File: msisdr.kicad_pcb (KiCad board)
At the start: 2 copper layers, 67 parts, among them J1 USB_OTG, J10 GPIO2, J11 GPIO3, J2 SMA_0_30MHZ, J3 SMA_30_60MHZ, J4 SMA_VHF2, J5 SMA_UHF, J6 SMA_VHF1, J7 VCC_GPIO, J8 GPIO0, J9 GPIO1, U1 msi2500, U2 msi001, U3 LP5900SDX-2.8, U4 AP7313-30SAG, Y1 24MHz

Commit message: update and fix bug
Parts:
- removed C39, C40, C41, C42: 10uF, Capacitors_SMD:C_0805
- added C23: 6800pF, Capacitors_SMD:C_0603, F.Cu at (152.2, 132.7)
- added C37: 10uF, Capacitors_SMD:C_0805, F.Cu at (145.6, 123.8)
- added D1: D, Diodes_SMD:D_0805, F.Cu at (159.9, 84.2)
- C10: value 10nF -> 18pF
- C15: value 100nF -> 10nF
- C17: value 1uF -> 100nF; footprint Capacitors_SMD:C_0805 -> Capacitors_SMD:C_0603
- C18: value 10nF -> 1uF; footprint Capacitors_SMD:C_0603 -> Capacitors_SMD:C_0805
- C21: value 6800pF -> 10nF
- C26: value 470nF -> 10nF; footprint Capacitors_SMD:C_0805 -> Capacitors_SMD:C_0603
- C27: value 1nF -> 470nF; footprint Capacitors_SMD:C_0603 -> Capacitors_SMD:C_0805
- C28: value 160pF -> 1nF
- C29: value 3.9pF -> 56pF
- C30: value 56pF -> 3.9pF
- C32: value 56pF -> 39pF
- C33: value 39pF -> 160pF
- C34: value 10uF -> 56pF; footprint Capacitors_SMD:C_0805 -> Capacitors_SMD:C_0603
- C35: value 10uF -> 100uF; footprint Capacitors_SMD:C_0805 -> Capacitors_THT:CP_Radial_D5.0mm_P2.50mm
- C7: value 1uF -> 10uF
- C8: value 18pF -> 1uF; footprint Capacitors_SMD:C_0603 -> Capacitors_SMD:C_0805
- J1: value USB_OTG -> VCC_GPIO; footprint Connectors:USB_Mini-B -> Connectors:Pin_d0.7mm_L6.5mm_W1.8mm_FlatFork
- J10: value GPIO2 -> SMA_VHF1; footprint Connectors:Pin_d0.7mm_L6.5mm_W1.8mm_FlatFork -> sma:SMA_OPL_EMPTYHEAD
- J11: value GPIO3 -> USB_OTG; footprint Connectors:Pin_d0.7mm_L6.5mm_W1.8mm_FlatFork -> Connectors:USB_Mini-B
- J2: value SMA_0_30MHZ -> GPIO0; footprint sma:SMA_OPL_EM -> Connectors:Pin_d0.7mm_L6.5mm_W1.8mm_FlatFork
- J3: value SMA_30_60MHZ -> GPIO1; footprint sma:SMA_OPL_EM -> Connectors:Pin_d0.7mm_L6.5mm_W1.8mm_FlatFork
- J4: value SMA_VHF2 -> GPIO2; footprint sma:SMA_OPL_EMPTYHEAD -> Connectors:Pin_d0.7mm_L6.5mm_W1.8mm_FlatFork
- J5: value SMA_UHF -> GPIO3; footprint sma:SMA_OPL_EMPTYHEAD -> Connectors:Pin_d0.7mm_L6.5mm_W1.8mm_FlatFork
- J6: value SMA_VHF1 -> SMA_0_30MHZ; footprint sma:SMA_OPL_EMPTYHEAD -> sma:SMA_OPL_EM
- J7: value VCC_GPIO -> SMA_30_60MHZ; footprint Connectors:Pin_d0.7mm_L6.5mm_W1.8mm_FlatFork -> sma:SMA_OPL_EM
- J8: value GPIO0 -> SMA_VHF2; footprint Connectors:Pin_d0.7mm_L6.5mm_W1.8mm_FlatFork -> sma:SMA_OPL_EMPTYHEAD
- J9: value GPIO1 -> SMA_UHF; footprint Connectors:Pin_d0.7mm_L6.5mm_W1.8mm_FlatFork -> sma:SMA_OPL_EMPTYHEAD
- L2: value 270nH -> 330nH
- L4: value 150nH -> 270nH
- L5: value 330nH -> 150nH
- moved J7 120.0 mm to (169.0, 159.8), turned to 90 degrees
- moved J10 108.6 mm to (178.3, 148.8)
- moved J8 105.7 mm to (156.9, 154.1)
- moved J9 103.1 mm to (167.2, 147.7)
- moved J6 84.6 mm to (147.8, 159.0), turned to 90 degrees
- moved J1 83.1 mm to (152.2, 132.7), turned to 0 degrees
- moved J5 68.6 mm to (152.2, 132.7)
- moved Y1 66.6 mm to (179.5, 136.6)
- moved U2 65.0 mm to (135.0, 158.5)
- moved C35 62.0 mm to (161.9, 89.4)
- moved C30 61.5 mm to (155.8, 132.6)
- moved C3 59.9 mm to (145.7, 139.1)
- moved C29 59.2 mm to (148.2, 132.5)
- moved C8 58.6 mm to (173.5, 126.6)
- moved C26 57.1 mm to (152.2, 132.7)
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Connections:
- C10 pad 2: VRF -> Net-(C10-Pad2)
- C12 pad 2: Net-(C12-Pad2) -> VRF
- C16 pad 1: HFPORT -> GND
- C17 pad 1: GND -> HFPORT
- C17 pad 2: VRF -> Net-(C17-Pad2)
- C18 pad 2: Net-(C18-Pad2) -> VRF
- C19 pad 2: VRF -> Net-(C19-Pad2)
- C20 pad 2: VDDI -> VRF
- C21 pad 1: Net-(C21-Pad1) -> GND
- C21 pad 2: Net-(C21-Pad2) -> VDDI
- C22 pad 2: Net-(C21-Pad2) -> Net-(C22-Pad2)
- C25 pad 1: Net-(C21-Pad1) -> GND
- C25 pad 2: GND -> VRF
- C26 pad 1: Net-(C26-Pad1) -> Net-(C22-Pad1)
- C26 pad 2: Net-(C26-Pad2) -> GND
- C27 pad 1: Net-(C26-Pad1) -> Net-(C27-Pad1)
- C27 pad 2: Net-(C26-Pad2) -> Net-(C27-Pad2)
- C28 pad 1: GND -> Net-(C27-Pad1)
- C28 pad 2: Net-(C28-Pad2) -> Net-(C27-Pad2)
- C29 pad 1: Net-(C29-Pad1) -> GND
- C29 pad 2: Net-(C29-Pad2) -> Net-(C27-Pad2)
- C30 pad 1: GND -> Net-(C30-Pad1)
- C30 pad 2: Net-(C26-Pad2) -> Net-(C30-Pad2)
- C32 pad 1: GND -> HFPORT
- C32 pad 2: HFPORT -> Net-(C30-Pad1)
- C33 pad 1: HFPORT -> GND
- C33 pad 2: Net-(C29-Pad1) -> Net-(C33-Pad2)
- C34 pad 1: VDIG -> GND
- C34 pad 2: GND -> HFPORT
- C36 pad 1: VDIG -> VRF
- C38 pad 1: VDIG -> Net-(C38-Pad1)
- C7 pad 1: Net-(C7-Pad1) -> VDIG
- C8 pad 1: GND -> Net-(C8-Pad1)
- C8 pad 2: Net-(C8-Pad2) -> GND
- J1 pad 1: Net-(C42-Pad1) -> Net-(J1-Pad1)
- J10 pad 1: Net-(J10-Pad1) -> VHF_50_120MHZ
- J11 pad 1: Net-(J11-Pad1) -> Net-(C38-Pad1)
- J2 pad 1: Net-(C26-Pad1) -> Net-(J2-Pad1)
- J4 pad 1: VHF_120_250MHZ -> Net-(J4-Pad1)
- J5 pad 1: UHF_400_1000MHZ -> Net-(J5-Pad1)
- J6 pad 1: VHF_50_120MHZ -> Net-(C27-Pad1)
- J8 pad 1: Net-(J8-Pad1) -> VHF_120_250MHZ
- J9 pad 1: Net-(J9-Pad1) -> UHF_400_1000MHZ
- L1 pad 1: Net-(C29-Pad2) -> Net-(C30-Pad2)
- L1 pad 2: Net-(J3-Pad1) -> Net-(J7-Pad1)
- L2 pad 1: Net-(L2-Pad1) -> Net-(C30-Pad1)
- L2 pad 2: Net-(C28-Pad2) -> Net-(C30-Pad2)
- L3 pad 1: Net-(C28-Pad2) -> Net-(C31-Pad2)
- L3 pad 2: Net-(C26-Pad2) -> Net-(C27-Pad2)
- L4 pad 1: Net-(C31-Pad2) -> Net-(L4-Pad1)
- L4 pad 2: Net-(L2-Pad1) -> Net-(C31-Pad2)
- L5 pad 1: Net-(C29-Pad1) -> Net-(C33-Pad2)
- L5 pad 2: Net-(C29-Pad2) -> Net-(L4-Pad1)
- L6 pad 2: Net-(C31-Pad2) -> Net-(C33-Pad2)
- R2 pad 1: Net-(C21-Pad1) -> Net-(C22-Pad1)
- R2 pad 2: Net-(C22-Pad1) -> Net-(C23-Pad1)
- U1 pad 1: Net-(J7-Pad1) -> Net-(J1-Pad1)
- U1 pad 16: Net-(C7-Pad1) -> Net-(C8-Pad1)
- U1 pad 19: USB-DP -> USB_DP
- U1 pad 2: Net-(J8-Pad1) -> Net-(J2-Pad1)
- U1 pad 20: USB-DM -> USB_DM
- U1 pad 22: Net-(C9-Pad2) -> Net-(C10-Pad2)
- U1 pad 23: Net-(C8-Pad2) -> Net-(C9-Pad2)
- U1 pad 3: Net-(J9-Pad1) -> Net-(J3-Pad1)
- U1 pad 4: Net-(J10-Pad1) -> Net-(J4-Pad1)
- U1 pad 5: Net-(J11-Pad1) -> Net-(J5-Pad1)
- U2 pad 14: Net-(C18-Pad2) -> Net-(C19-Pad2)
- U2 pad 15: Net-(C18-Pad2) -> Net-(C19-Pad2)
- U2 pad 18: Net-(C18-Pad2) -> Net-(C19-Pad2)
- U2 pad 19: Net-(C18-Pad2) -> Net-(C19-Pad2)
- U2 pad 26: Net-(C22-Pad1) -> Net-(C23-Pad1)
- U2 pad 27: Net-(C21-Pad2) -> Net-(C22-Pad2)
- U2 pad 28: Net-(C21-Pad1) -> Net-(C22-Pad1)
- U2 pad 39: Net-(C16-Pad2) -> Net-(C17-Pad2)
- U2 pad 4: Net-(C13-Pad2) -> Net-(C14-Pad2)
- U2 pad 40: Net-(C15-Pad2) -> Net-(C16-Pad2)
- U2 pad 7: Net-(C14-Pad2) -> Net-(C15-Pad2)
- U2 pad 9: Net-(C12-Pad2) -> Net-(C13-Pad2)
- U3 pad 6: Net-(C42-Pad1) -> Net-(C38-Pad1)
- U4 pad 1: Net-(C42-Pad1) -> Net-(C38-Pad1)
- Y1 pad 1: Net-(C8-Pad2) -> Net-(C9-Pad2)
- Y1 pad 2: Net-(C9-Pad2) -> Net-(C10-Pad2)
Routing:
- net GND: track 0.00 -> 37.7 mm, vias 0 -> 2
- net USB_DP: track 0.00 -> 35.3 mm, vias 0 -> 4
- net USB_DM: track 0.00 -> 32.9 mm
- net Net-(C38-Pad1): track 0.00 -> 21.2 mm
- net VDIG: track 0.00 -> 13.7 mm
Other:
- net class Default: clearance 0.2 -> 0.15; trace_width 0.25 -> 0.2
- net class GND added: clearance 0.2, trace_width 0.2, via_dia 0.6, via_drill 0.4
- net class VDIG added: clearance 0.2, trace_width 0.2, via_dia 0.6, via_drill 0.4
- net class VRF added: clearance 0.2, trace_width 0.2, via_dia 0.6, via_drill 0.4
- rule trace_clearance: 0.2 -> 0.15

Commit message: update pcb
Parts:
- moved C24 67.2 mm to (85.1, 127.4)
- moved C26 61.7 mm to (90.7, 128.1)
- moved Y1 54.1 mm to (145.2, 94.6), turned to 90 degrees
- moved C29 50.9 mm to (98.9, 120.3)
- moved C30 50.1 mm to (109.6, 113.2)
- moved C34 49.4 mm to (105.3, 129.2)
- moved C31 49.4 mm to (107.8, 121.9)
- moved C27 49.4 mm to (91.4, 117.0)
- moved C37 49.4 mm to (96.8, 116.4)
- moved C32 49.4 mm to (111.9, 121.5)
- moved C28 49.4 mm to (92.3, 123.9)
- moved C33 49.4 mm to (117.4, 125.2)
- moved C3 47.4 mm to (163.0, 95.0)
- moved C10 46.2 mm to (138.3, 88.7)
- moved R1 43.2 mm to (153.4, 89.6)
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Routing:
- net VRF: track 0.00 -> 129.1 mm, vias 0 -> 2
- net GND: track 37.7 -> 134.6 mm, vias 2 -> 6
- net VDIG: track 13.7 -> 103.0 mm, vias 0 -> 5
- net VDDI: track 0.00 -> 57.3 mm, vias 0 -> 6
- net I_IN_P: track 0.00 -> 43.9 mm, vias 0 -> 2
- net I_IN_N: track 0.00 -> 41.2 mm, vias 0 -> 2
- net REFCLK: track 0.00 -> 41.1 mm, vias 0 -> 2
- net SPI_DATA: track 0.00 -> 35.2 mm, vias 0 -> 2
- net SPI_CLK: track 0.00 -> 34.6 mm, vias 0 -> 2
- net SPI_LAT: track 0.00 -> 34.5 mm
- net Q_IN_N: track 0.00 -> 30.1 mm
- net Q_IN_P: track 0.00 -> 29.3 mm
- net Net-(J5-Pad1): track 0.00 -> 27.4 mm, vias 0 -> 1
- net Net-(J4-Pad1): track 0.00 -> 25.1 mm, vias 0 -> 1
- net Net-(J3-Pad1): track 0.00 -> 22.8 mm, vias 0 -> 1
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
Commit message: update pcb
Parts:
- moved C26 61.6 mm to (151.8, 120.8)
- moved C24 58.7 mm to (143.6, 132.5), turned to 90 degrees
- moved C16 4.35 mm to (150.8, 137.5)
- moved J10 3.44 mm to (180.2, 151.6), turned to 90 degrees
- moved C17 2.76 mm to (147.1, 137.4)
- moved C14 2.59 mm to (156.8, 137.5)
- moved C12 2.59 mm to (154.4, 137.5)
- moved C15 2.59 mm to (159.2, 137.5)
- moved J8 2.58 mm to (159.0, 155.6), turned to 90 degrees
- moved J9 2.10 mm to (168.9, 148.9), turned to 90 degrees
- moved R2 1.86 mm to (155.4, 114.0)
- moved C11 1.20 mm to (147.1, 132.5)
- turned C20 to 180 degrees
- turned C25 to 180 degrees
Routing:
- net GND: track 134.6 -> 216.4 mm, vias 6 -> 11
- net VRF: track 129.1 -> 147.5 mm
- net Net-(C23-Pad1): track 0.00 -> 18.1 mm, vias 0 -> 2
- net Net-(C22-Pad1): track 0.00 -> 16.4 mm, vias 0 -> 2
- net Net-(C22-Pad2): track 0.00 -> 11.9 mm, vias 0 -> 2
- net Net-(C38-Pad1): track 21.2 -> 29.3 mm, vias 0 -> 2
- net Net-(C13-Pad2): track 0.00 -> 6.31 mm
- net VDDI: track 57.3 -> 61.0 mm

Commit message: finish pcb v1
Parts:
- moved C37 48.2 mm to (125.4, 77.7), turned to 90 degrees
- moved J8 44.1 mm to (120.2, 134.6)
- moved C30 39.5 mm to (148.1, 122.2), turned to 270 degrees
- moved C28 39.0 mm to (131.2, 126.6), turned to 90 degrees
- moved C29 37.0 mm to (135.4, 126.4), turned to 90 degrees
- moved C27 36.8 mm to (126.9, 126.6), turned to 90 degrees
- moved J9 35.2 mm to (136.7, 134.6)
- moved J7 34.9 mm to (144.8, 134.6)
- moved J10 32.4 mm to (152.5, 134.6)
- moved C17 31.2 mm to (127.6, 113.0)
- moved D4 31.2 mm to (131.4, 55.1)
- moved C10 31.2 mm to (118.9, 64.3)
- moved C11 31.2 mm to (127.7, 108.1)
- moved C18 31.2 mm to (149.8, 76.5)
- moved C22 31.2 mm to (132.4, 94.1)
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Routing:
- net GND: track 216.4 -> 266.4 mm, vias 11 -> 15
- net VHF_50_120MHZ: track 0.00 -> 33.3 mm, vias 0 -> 2
- net VHF_120_250MHZ: track 0.00 -> 31.4 mm, vias 0 -> 2
- net UHF_400_1000MHZ: track 0.00 -> 24.9 mm, vias 0 -> 2
- net HFPORT: track 0.00 -> 18.5 mm
- net Net-(C14-Pad2): track 0.00 -> 16.3 mm, vias 0 -> 2
- net Net-(C15-Pad2): track 0.00 -> 13.5 mm, vias 0 -> 2
- net Net-(C33-Pad2): track 0.00 -> 12.9 mm
- net Net-(C27-Pad2): track 0.00 -> 12.5 mm
- net Net-(C31-Pad2): track 0.00 -> 10.1 mm
- net Net-(C27-Pad1): track 0.00 -> 8.98 mm
- net Net-(C17-Pad2): track 0.00 -> 8.02 mm, vias 0 -> 2
- net Net-(C30-Pad1): track 0.00 -> 7.97 mm
- net VRF: track 147.5 -> 154.8 mm
- net Net-(C16-Pad2): track 0.00 -> 6.97 mm, vias 0 -> 2
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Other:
- board outline added: 46.3 x 90.7 mm

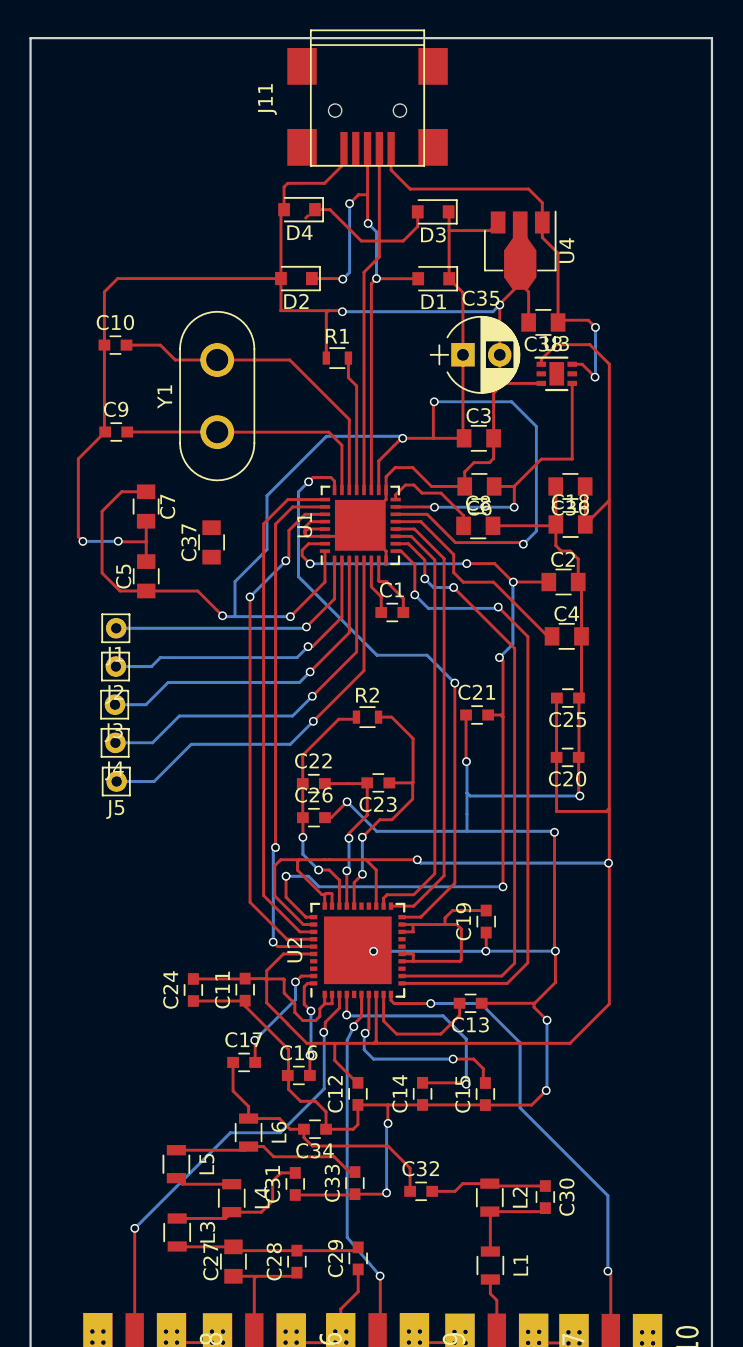
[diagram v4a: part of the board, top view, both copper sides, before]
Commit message: add machine hole
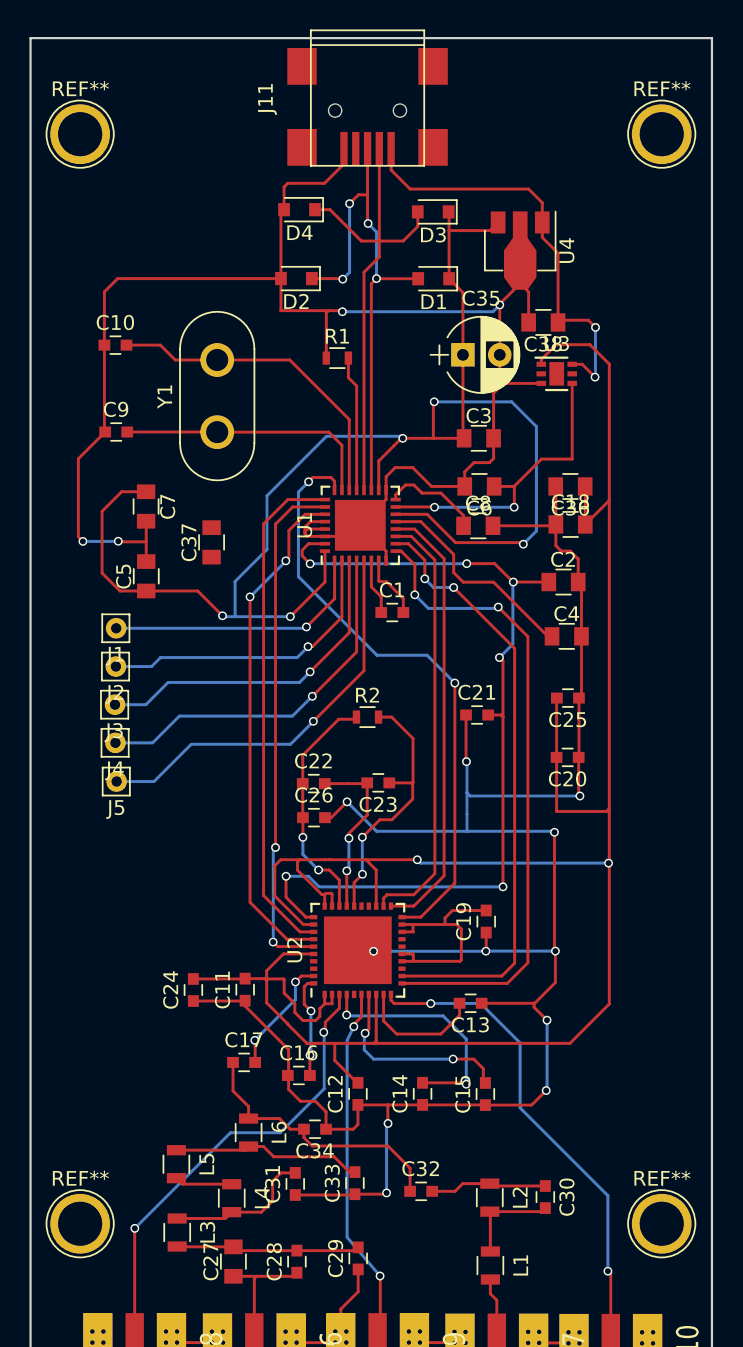
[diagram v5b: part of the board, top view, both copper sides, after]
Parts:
- added REF**: 1pin, Connectors:1pin, F.Cu at (156.0, 124.0)
- added REF**: 1pin, Connectors:1pin, F.Cu at (116.5, 124.0)
- added REF**: 1pin, Connectors:1pin, F.Cu at (156.0, 50.0)
- added REF**: 1pin, Connectors:1pin, F.Cu at (116.5, 50.0)
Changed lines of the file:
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@@
     (links 234)
     (no_connects 33)
-    (area 88.930476 66.854999 186.92615 169.172501)
+    (area 113.056599 42.470999 159.490481 144.007101)
     (thickness 1.6)
     (drawings 5)
-    (tracks 733)
+    (tracks 732)
     (zones 0)
-    (modules 66)
+    (modules 70)
     (nets 62)
   )
@@
     (uvia_drill 0.1)
   )
+  (module Connectors:1pin (layer F.Cu)
+    (at 156 124)
+    (descr "module 1 pin (ou trou mecanique de percage)")
+    (tags DEV)
+    (fp_text reference REF** (at 0 -3.048) (layer F.SilkS)
+      (effects (font (size 1 1) (thickness 0.15)))
+    )
+    (fp_text value 1pin (at 0 3) (layer F.Fab)
+      (effects (font (size 1 1) (thickness 0.15)))
+    )
+    (fp_circle (center 0 0) (end 2 0.8) (layer F.Fab) (width 0.1))
+    (fp_circle (center 0 0) (end 2.6 0) (layer F.CrtYd) (width 0.05))
+    (fp_circle (center 0 0) (end 0 -2.286) (layer F.SilkS) (width 0.12))
+    (pad 1 thru_hole circle (at 0 0) (size 4.064 4.064) (drill 3) (layers *.Cu *.Mask))
+  )
+  (module Connectors:1pin (layer F.Cu)
+    (at 116.5 124)
+    (descr "module 1 pin (ou trou mecanique de percage)")
+    (tags DEV)
+    (fp_text reference REF** (at 0 -3.048) (layer F.SilkS)
+      (effects (font (size 1 1) (thickness 0.15)))
+    )
+    (fp_text value 1pin (at 0 3) (layer F.Fab)
+      (effects (font (size 1 1) (thickness 0.15)))
+    )
+    (fp_circle (center 0 0) (end 2 0.8) (layer F.Fab) (width 0.1))
+    (fp_circle (center 0 0) (end 2.6 0) (layer F.CrtYd) (width 0.05))
+    (fp_circle (center 0 0) (end 0 -2.286) (layer F.SilkS) (width 0.12))
+    (pad 1 thru_hole circle (at 0 0) (size 4.064 4.064) (drill 3) (layers *.Cu *.Mask))
+  )
+  (module Connectors:1pin (layer F.Cu)
+    (at 156 50)
+    (descr "module 1 pin (ou trou mecanique de percage)")
+    (tags DEV)
+    (fp_text reference REF** (at 0 -3.048) (layer F.SilkS)
+      (effects (font (size 1 1) (thickness 0.15)))
+    )
+    (fp_text value 1pin (at 0 3) (layer F.Fab)
+      (effects (font (size 1 1) (thickness 0.15)))
+    )
+    (fp_circle (center 0 0) (end 2 0.8) (layer F.Fab) (width 0.1))
+    (fp_circle (center 0 0) (end 2.6 0) (layer F.CrtYd) (width 0.05))
+    (fp_circle (center 0 0) (end 0 -2.286) (layer F.SilkS) (width 0.12))
+    (pad 1 thru_hole circle (at 0 0) (size 4.064 4.064) (drill 3) (layers *.Cu *.Mask))
+  )
+  (module Connectors:1pin (layer F.Cu)
+    (at 116.5 50)
+    (descr "module 1 pin (ou trou mecanique de percage)")
+    (tags DEV)
+    (fp_text reference REF** (at 0 -3.048) (layer F.SilkS)
+      (effects (font (size 1 1) (thickness 0.15)))
+    )
+    (fp_text value 1pin (at 0 3) (layer F.Fab)
+      (effects (font (size 1 1) (thickness 0.15)))
+    )
+    (fp_circle (center 0 0) (end 2 0.8) (layer F.Fab) (width 0.1))
+    (fp_circle (center 0 0) (end 2.6 0) (layer F.CrtYd) (width 0.05))
+    (fp_circle (center 0 0) (end 0 -2.286) (layer F.SilkS) (width 0.12))
+    (pad 1 thru_hole circle (at 0 0) (size 4.064 4.064) (drill 3) (layers *.Cu *.Mask))
+  )
   (module Capacitors_SMD:C_0603 (layer F.Cu)
     (at 137.699 82.486)
@@
       (effects (font (size 1.5 1.2) (thickness 0.2)))
     )
-    (fp_text value SMA_0_30MHZ (at 0 0 90) (layer F.SilkS) hide
+    (fp_text value SMA_0_30MHZ (at 6.7378 -3.3356 90) (layer F.SilkS) hide
       (effects (font (size 1.5 1.2) (thickness 0.2)))
     )
@@
       (effects (font (size 1.5 1.2) (thickness 0.2)))
     )
-    (fp_text value SMA_30_60MHZ (at 0 0 90) (layer F.SilkS) hide
+    (fp_text value SMA_30_60MHZ (at 7.5565 -0.16002 90) (layer F.SilkS) hide
       (effects (font (size 1.5 1.2) (thickness 0.2)))
     )
@@
       (effects (font (size 1.5 1.2) (thickness 0.2)))
     )
-    (fp_text value SMA_VHF2 (at 2.54 -5.08 90) (layer F.SilkS) hide
+    (fp_text value SMA_VHF2 (at 5.26288 -5.48386 90) (layer F.SilkS) hide
       (effects (font (size 1.5 1.2) (thickness 0.2)))
     )
@@
       (effects (font (size 1.5 1.2) (thickness 0.2)))
     )
-    (fp_text value SMA_UHF (at 2.54 -5.08 90) (layer F.SilkS) hide
+    (fp_text value SMA_UHF (at 4.7752 2.3368 90) (layer F.SilkS) hide
       (effects (font (size 1.5 1.2) (thickness 0.2)))
     )
@@
       (effects (font (size 1.5 1.2) (thickness 0.2)))
     )
-    (fp_text value SMA_VHF1 (at 2.54 -5.08 90) (layer F.SilkS) hide
+    (fp_text value SMA_VHF1 (at 9.62914 -0.6096 90) (layer F.SilkS) hide
       (effects (font (size 1.5 1.2) (thickness 0.2)))
     )
@@
   (gr_line (start 159.4104 43.47464) (end 113.1316 43.47464) (angle 90) (layer Edge.Cuts) (width 0.15))
   (gr_line (start 159.4104 134.112) (end 159.4104 43.47464) (angle 90) (layer Edge.Cuts) (width 0.15))
-  (segment (start 131.819 55.696) (end 131.979 55.536) (width 0.2) (layer F.Cu) (net 0))
   (segment (start 136.779 78.966) (end 136.779 80.336) (width 0.2) (layer F.Cu) (net 1))
   (segment (start 136.779 80.336) (end 136.829 80.386) (width 0.2) (layer F.Cu) (net 1))

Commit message: finish drc
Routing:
- net GND: track 266.4 -> 398.2 mm, vias 15 -> 19
- net Net-(J11-Pad6): track 0.00 -> 19.9 mm
- net VDIG: track 103.0 -> 105.7 mm
